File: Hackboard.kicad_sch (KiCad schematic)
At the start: 41 parts, among them J1 Barrel_Jack, J2 USB_C_Receptacle_USB2.0_16P, J3 Micro_SD_Card, J4 Conn_01x30_Pin, J5 Conn_01x30_Pin, SW1 SW_MEC_5E, U1 STM32L476RGT6, U2 AP63205WU, U3 NCP164CSN330T1G, U4 USBLC6-2SC6

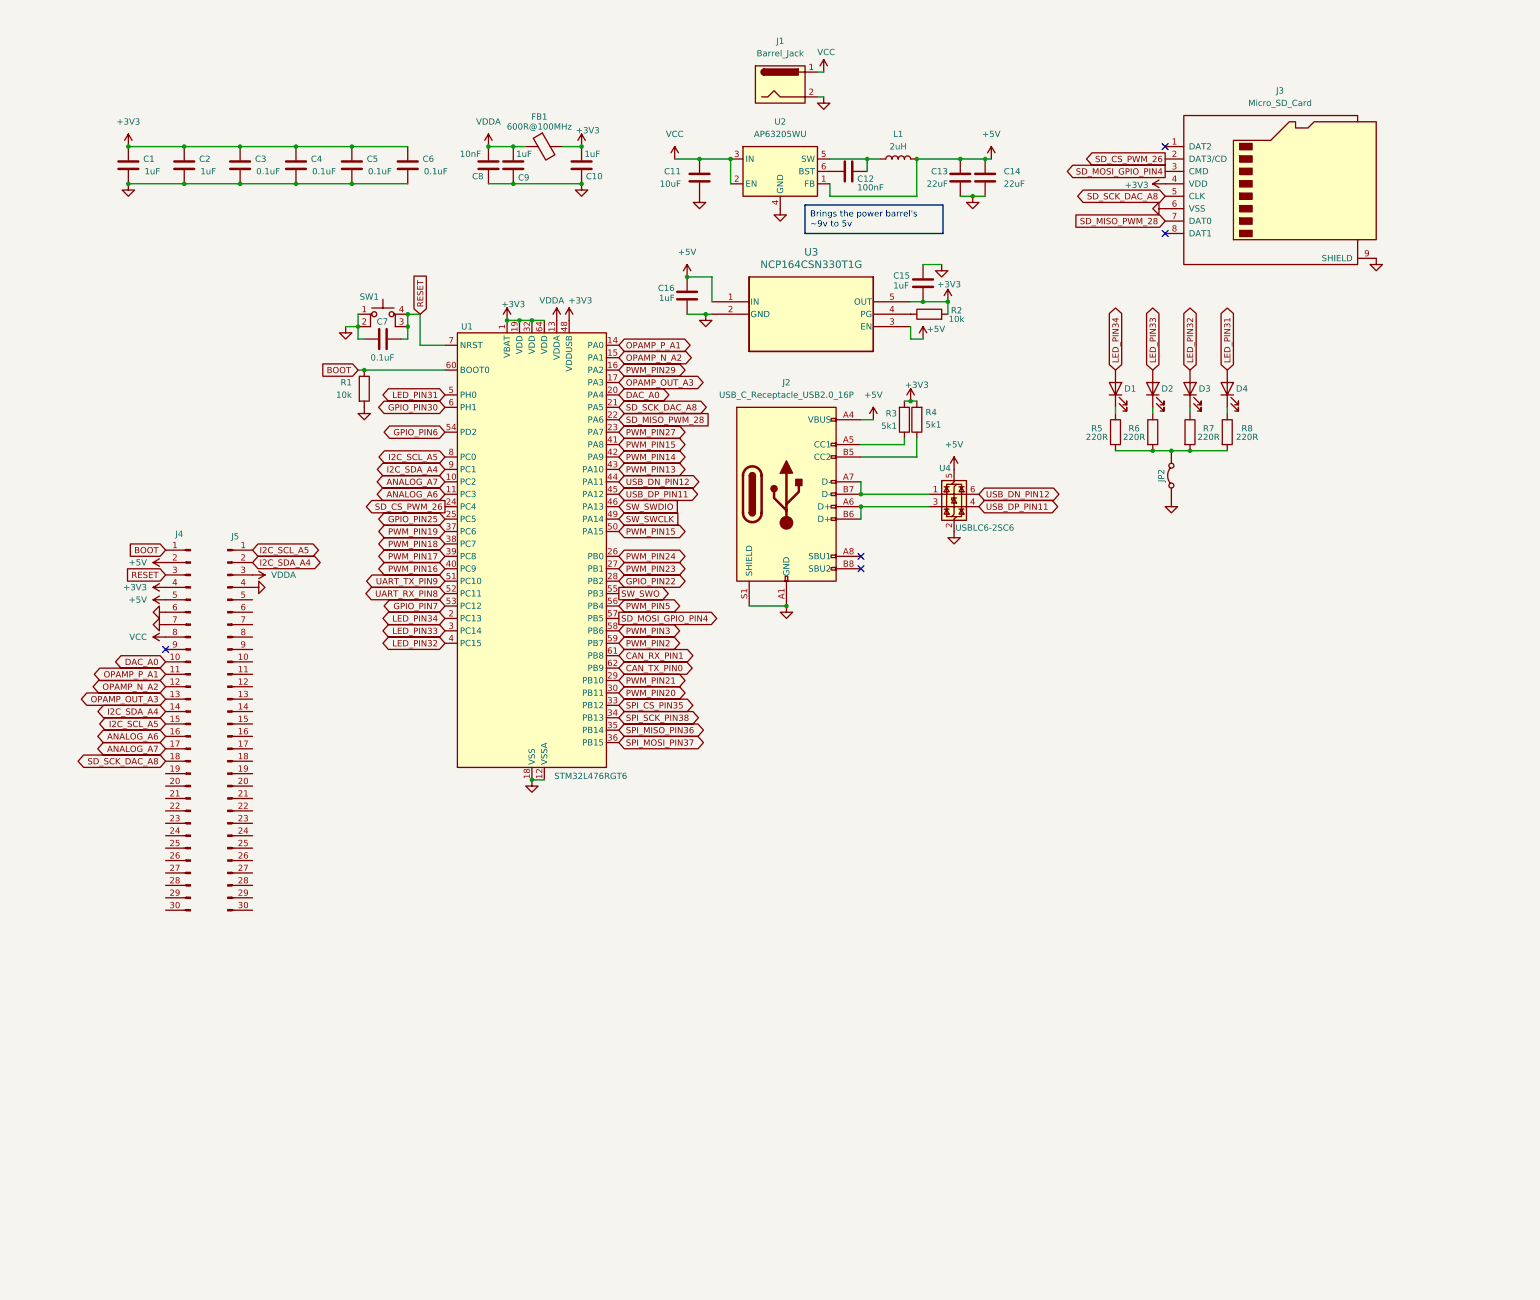
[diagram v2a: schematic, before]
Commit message: Make some power changes, add logic shifters
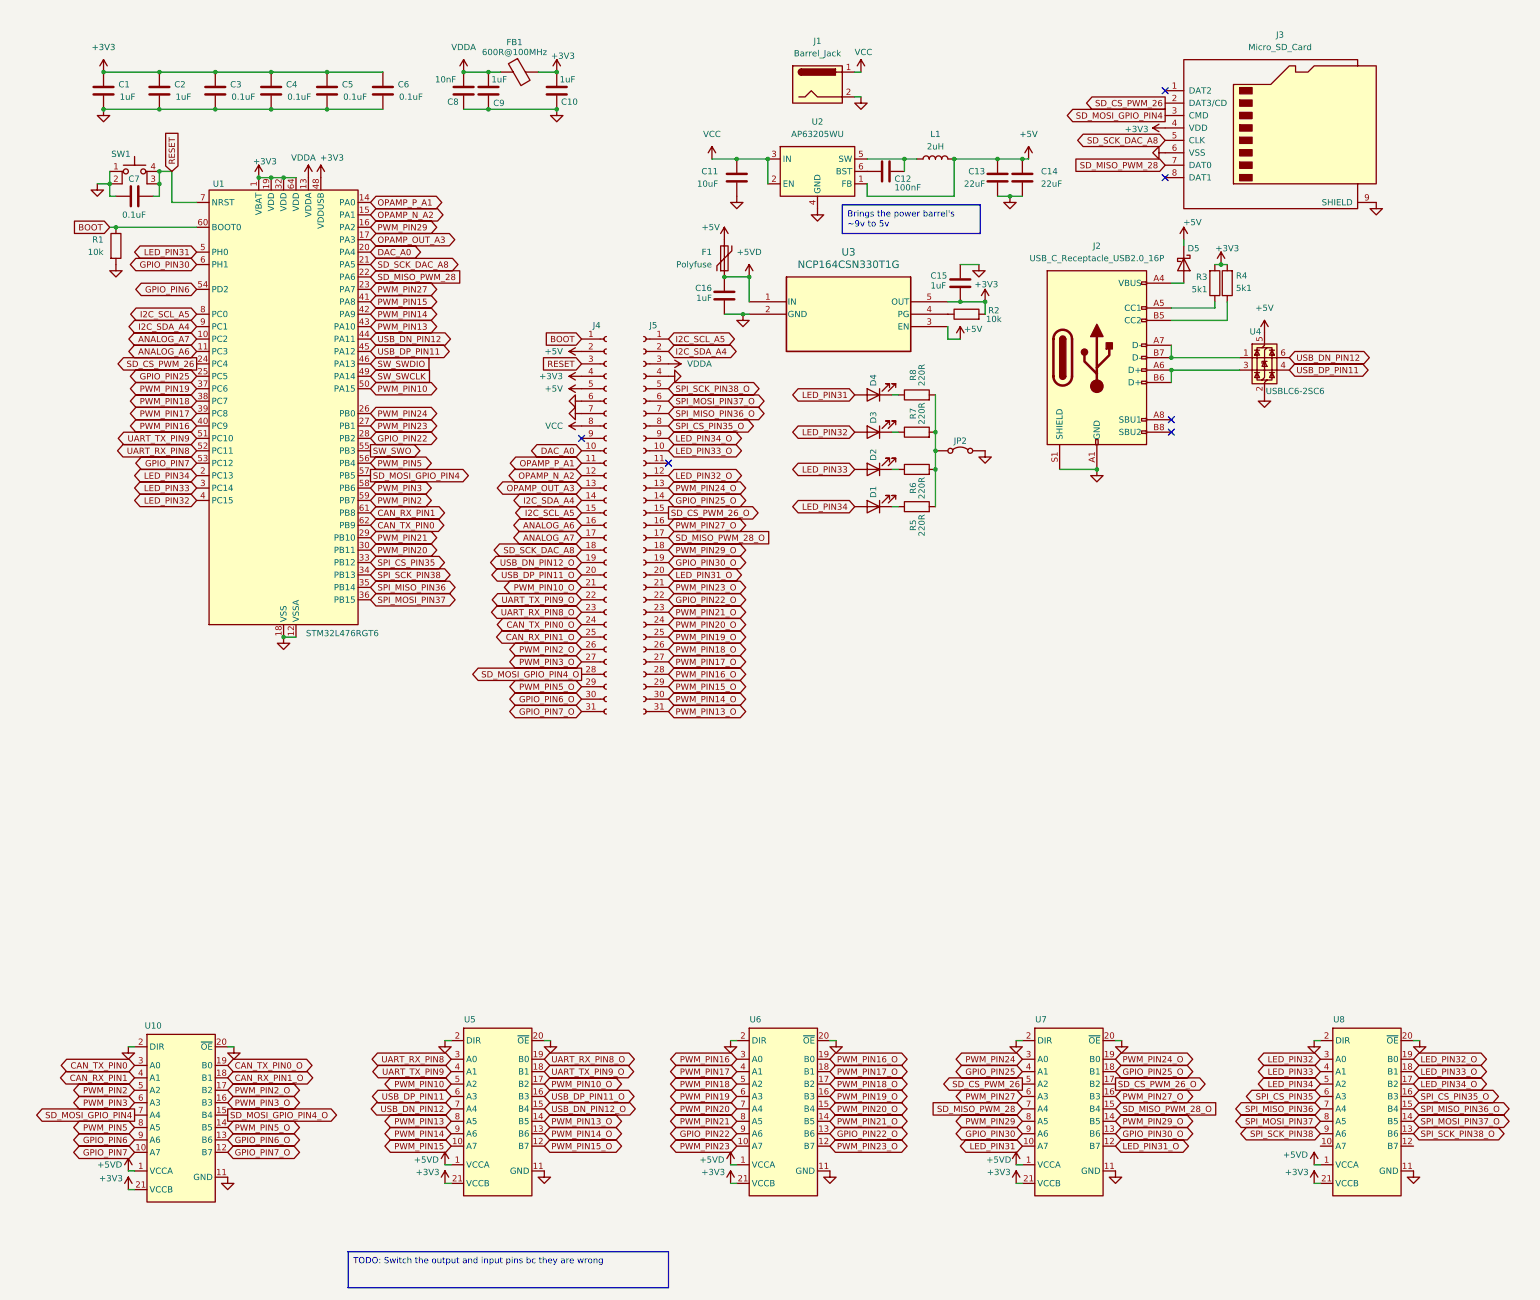
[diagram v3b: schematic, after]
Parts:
- removed J4, J5: Conn_01x30_Pin, symbol Connector:Conn_01x30_Pin
- added D5: D_Schottky, symbol Device:D_Schottky
- added F1: Polyfuse, symbol Device:Polyfuse
- added J4, J5: Conn_01x31_Socket, symbol Connector:Conn_01x31_Socket
- added U10, U5, U6, U7, U8: ~, symbol 74LVC4245A:74LVC4245A
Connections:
- net +3V3: now also J4.4 (Pin_4), U10.21 (VCCB), U5.21 (VCCB), U6.21 (VCCB), U7.21 (VCCB), U8.21 (VCCB)
- net +5V: now also D5.1 (K), F1.2, J4.2 (Pin_2), J4.5 (Pin_5); no longer C16.1, J2.A4 (VBUS), J2.A9 (VBUS), J2.B4 (VBUS), J2.B9 (VBUS), U3.1 (IN)
- net ANALOG_A6: now also J4.16 (Pin_16)
- net ANALOG_A7: now also J4.17 (Pin_17)
- net BOOT: now also J4.1 (Pin_1)
- net CAN_RX_PIN1: now also U10.4 (A1)
- net CAN_TX_PIN0: now also U10.3 (A0)
- net DAC_A0: now also J4.10 (Pin_10)
- net GND: now also J4.6 (Pin_6), J4.7 (Pin_7), J5.4 (Pin_4), U10.11 (GND), U10.2 (DIR), U10.20 (~{OE}), U5.11 (GND), U5.2 (DIR), U5.20 (~{OE}), U6.11 (GND), U6.2 (DIR), U6.20 (~{OE}), U7.11 (GND), U7.2 (DIR), U7.20 (~{OE}), U8.11 (GND), U8.2 (DIR), U8.20 (~{OE})
- net GPIO_PIN22: now also U6.9 (A6)
- net GPIO_PIN25: now also U7.4 (A1)
- net GPIO_PIN30: now also U7.9 (A6)
- net GPIO_PIN6: now also U10.9 (A6)
- net GPIO_PIN7: now also U10.10 (A7)
- net I2C_SCL_A5: now also J4.15 (Pin_15), J5.1 (Pin_1)
- net I2C_SDA_A4: now also J4.14 (Pin_14), J5.2 (Pin_2)
- net LED_PIN31: now also U7.10 (A7)
- net LED_PIN32: now also U8.3 (A0)
- net LED_PIN33: now also U8.4 (A1)
- net LED_PIN34: now also U8.5 (A2)
- net OPAMP_N_A2: now also J4.12 (Pin_12)
- net OPAMP_OUT_A3: now also J4.13 (Pin_13)
- net OPAMP_P_A1: now also J4.11 (Pin_11)
- net PWM_PIN13: now also U5.8 (A5)
- net PWM_PIN14: now also U5.9 (A6)
- net PWM_PIN15: now also U5.10 (A7); no longer U1.50 (PA15)
- net PWM_PIN16: now also U6.3 (A0)
- net PWM_PIN17: now also U6.4 (A1)
- net PWM_PIN18: now also U6.5 (A2)
- net PWM_PIN19: now also U6.6 (A3)
- net PWM_PIN2: now also U10.5 (A2)
- net PWM_PIN20: now also U6.7 (A4)
- net PWM_PIN21: now also U6.8 (A5)
- net PWM_PIN23: now also U6.10 (A7)
- net PWM_PIN24: now also U7.3 (A0)
- net PWM_PIN27: now also U7.6 (A3)
- net PWM_PIN29: now also U7.8 (A5)
- net PWM_PIN3: now also U10.6 (A3)
- net PWM_PIN5: now also U10.8 (A5)
- net RESET: now also J4.3 (Pin_3)
- net SD_CS_PWM_26: now also U7.5 (A2)
- net SD_MISO_PWM_28: now also U7.7 (A4)
- net SD_MOSI_GPIO_PIN4: now also U10.7 (A4)
- net SD_SCK_DAC_A8: now also J4.18 (Pin_18)
- net SPI_CS_PIN35: now also U8.6 (A3)
- net SPI_MISO_PIN36: now also U8.7 (A4)
- net SPI_MOSI_PIN37: now also U8.8 (A5)
- net SPI_SCK_PIN38: now also U8.9 (A6)
- net UART_RX_PIN8: now also U5.3 (A0)
- net UART_TX_PIN9: now also U5.4 (A1)
- net USB_DN_PIN12: now also U5.7 (A4)
- net USB_DP_PIN11: now also U5.6 (A3)
- net VCC: now also J4.8 (Pin_8)
- net VDDA: now also J5.3 (Pin_3)
- new net: D5.2 (A), J2.A4 (VBUS), J2.A9 (VBUS), J2.B4 (VBUS), J2.B9 (VBUS)
- new net +5VD: C16.1, F1.1, U10.1 (VCCA), U3.1 (IN), U5.1 (VCCA), U6.1 (VCCA), U7.1 (VCCA), U8.1 (VCCA)
- new net CAN_RX_PIN1_O: J4.25 (Pin_25), U10.18 (B1)
- new net CAN_TX_PIN0_O: J4.24 (Pin_24), U10.19 (B0)
- new net GPIO_PIN22_O: U6.13 (B6)
- new net GPIO_PIN25_O: J5.14 (Pin_14), U7.18 (B1)
- new net GPIO_PIN30_O: J5.19 (Pin_19), U7.13 (B6)
- new net GPIO_PIN6_O: J4.30 (Pin_30), U10.13 (B6)
- new net GPIO_PIN7_O: J4.31 (Pin_31), U10.12 (B7)
- new net LED_PIN31_O: J5.20 (Pin_20), U7.12 (B7)
- new net LED_PIN32_O: J5.12 (Pin_12), U8.19 (B0)
- new net LED_PIN33_O: J5.10 (Pin_10), U8.18 (B1)
- new net LED_PIN34_O: J5.9 (Pin_9), U8.17 (B2)
- new net PWM_PIN10: U1.50 (PA15), U5.5 (A2)
- new net PWM_PIN10_O: J4.21 (Pin_21), U5.17 (B2)
- new net PWM_PIN13_O: J5.31 (Pin_31), U5.14 (B5)
- new net PWM_PIN14_O: J5.30 (Pin_30), U5.13 (B6)
- new net PWM_PIN15_O: J5.29 (Pin_29), U5.12 (B7)
- new net PWM_PIN16_O: U6.19 (B0)
- new net PWM_PIN17_O: U6.18 (B1)
- new net PWM_PIN18_O: U6.17 (B2)
- new net PWM_PIN19_O: U6.16 (B3)
- new net PWM_PIN20_O: U6.15 (B4)
- new net PWM_PIN21_O: U6.14 (B5)
- new net PWM_PIN23_O: U6.12 (B7)
- new net PWM_PIN24_O: J5.13 (Pin_13), U7.19 (B0)
- new net PWM_PIN27_O: J5.16 (Pin_16), U7.16 (B3)
- new net PWM_PIN29_O: J5.18 (Pin_18), U7.14 (B5)
- new net PWM_PIN2_O: J4.26 (Pin_26), U10.17 (B2)
- new net PWM_PIN3_O: J4.27 (Pin_27), U10.16 (B3)
- new net PWM_PIN5_O: J4.29 (Pin_29), U10.14 (B5)
- new net SD_CS_PWM_26_O: J5.15 (Pin_15), U7.17 (B2)
- new net SD_MISO_PWM_28_O: J5.17 (Pin_17), U7.15 (B4)
- new net SD_MOSI_GPIO_PIN4_O: J4.28 (Pin_28), U10.15 (B4)
- new net SPI_CS_PIN35_O: J5.8 (Pin_8), U8.16 (B3)
- new net SPI_MISO_PIN36_O: J5.7 (Pin_7), U8.15 (B4)
- new net SPI_MOSI_PIN37_O: J5.6 (Pin_6), U8.14 (B5)
- new net SPI_SCK_PIN38_O: J5.5 (Pin_5), U8.13 (B6)
- new net UART_RX_PIN8_O: J4.23 (Pin_23), U5.19 (B0)
- new net UART_TX_PIN9_O: J4.22 (Pin_22), U5.18 (B1)
- new net USB_DN_PIN12_O: J4.19 (Pin_19), U5.15 (B4)
- new net USB_DP_PIN11_O: J4.20 (Pin_20), U5.16 (B3)
- no-connect marks 5 -> 6
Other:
- moved on the sheet: C1, C10, C11, C12, C13, C14, C15, C16, C2, C3, C4, C5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
